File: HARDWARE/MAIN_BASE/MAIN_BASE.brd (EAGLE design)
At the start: 174 x 92.7 mm, 2 parts

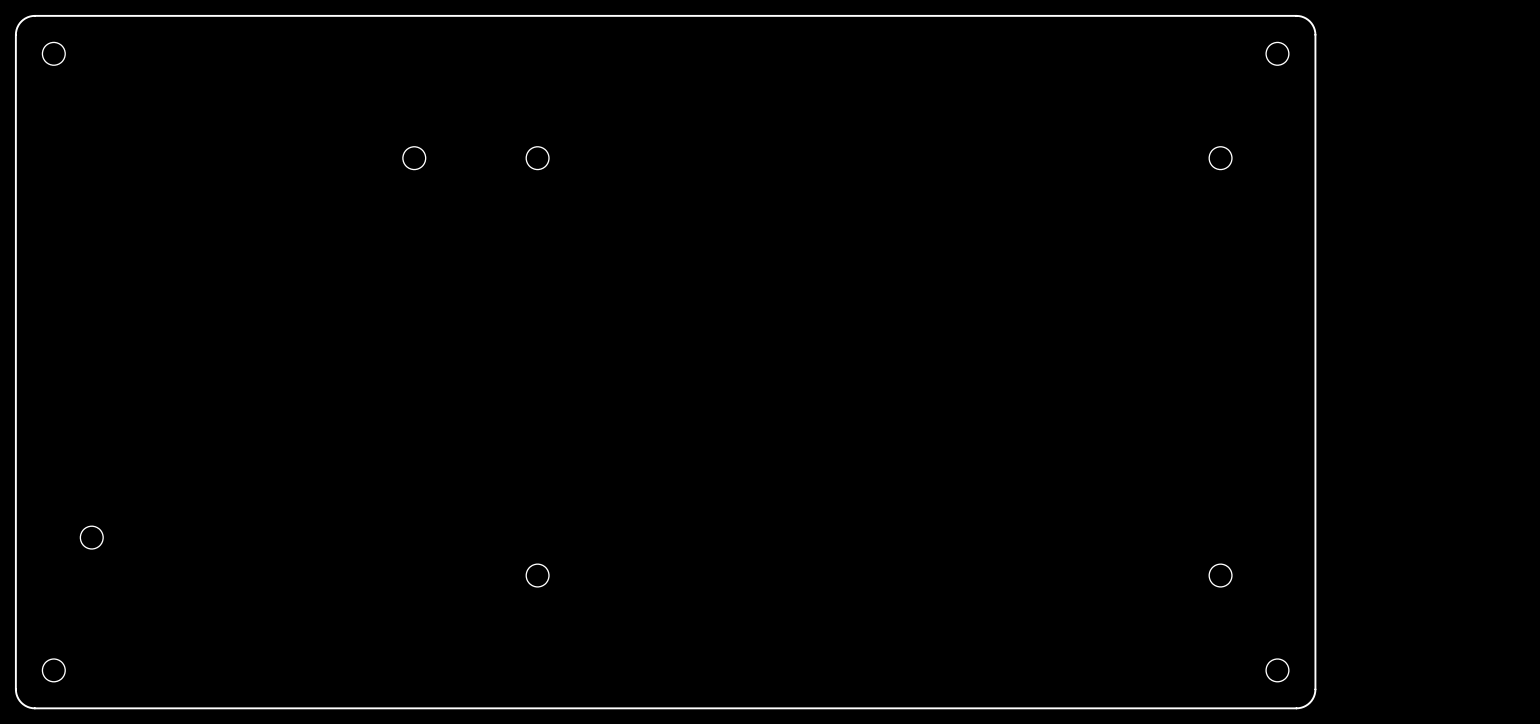
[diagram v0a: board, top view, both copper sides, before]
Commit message: added noisey cricket to base
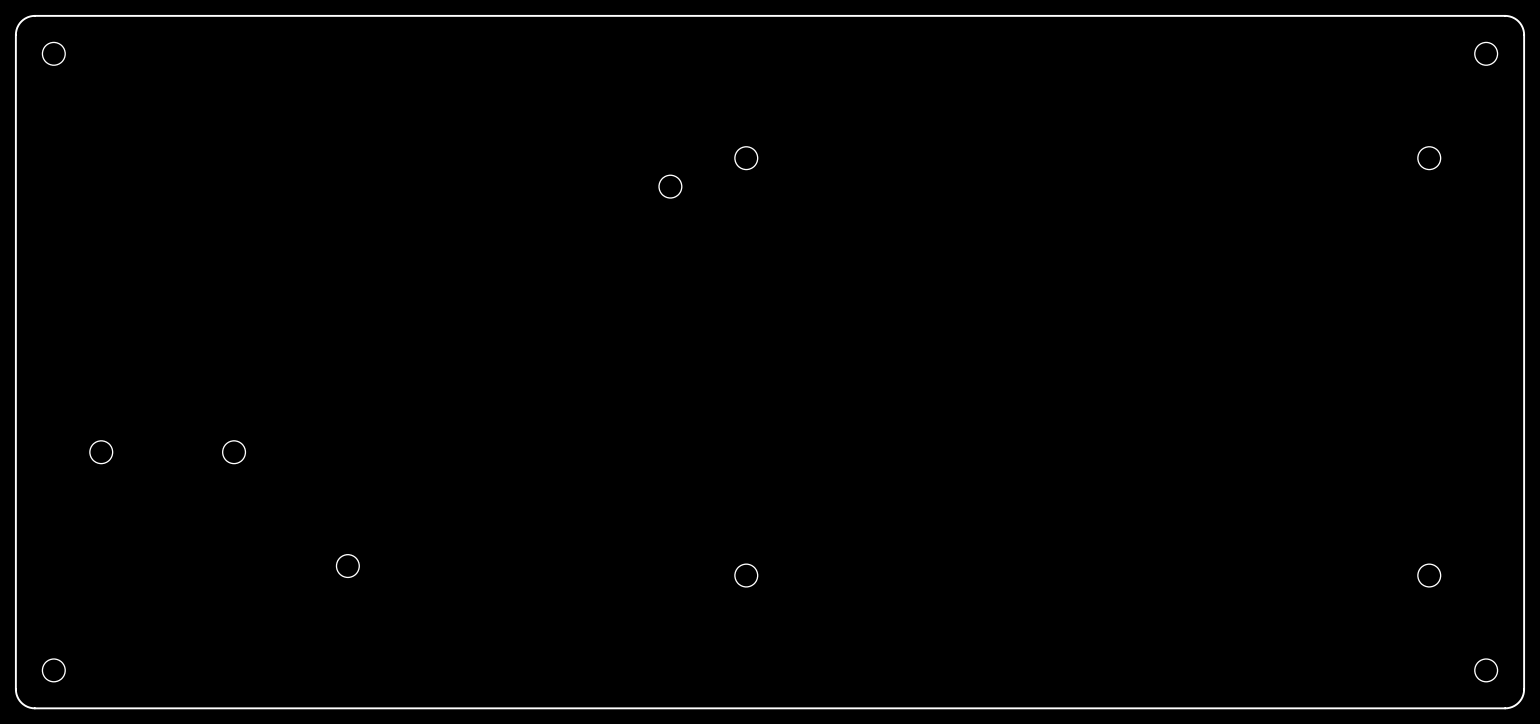
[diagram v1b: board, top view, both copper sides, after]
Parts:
- added E$3: (no value), simon_jumps:NOISY_CRICKET
- moved E$1 32.0 mm to (64.8, 48.3), turned to 180 degrees
- moved E$2 27.9 mm to (142.2, 45.7)
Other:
- board size 174 x 92.7 mm -> 201.9 x 92.7 mm
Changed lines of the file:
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@@
 <board>
 <plain>
-<wire x1="173.99" y1="90.17" x2="173.99" y2="2.54" width="0.254" layer="20"/>
-<wire x1="173.99" y1="2.54" x2="171.45" y2="0" width="0.254" layer="20" curve="-90"/>
-<wire x1="171.45" y1="0" x2="2.54" y2="0" width="0.254" layer="20"/>
+<wire x1="201.93" y1="90.17" x2="201.93" y2="2.54" width="0.254" layer="20"/>
+<wire x1="201.93" y1="2.54" x2="199.39" y2="0" width="0.254" layer="20" curve="-90"/>
+<wire x1="199.39" y1="0" x2="2.54" y2="0" width="0.254" layer="20"/>
 <wire x1="2.54" y1="0" x2="0" y2="2.54" width="0.254" layer="20" curve="-90"/>
 <wire x1="0" y1="2.54" x2="0" y2="90.17" width="0.254" layer="20"/>
 <wire x1="0" y1="90.17" x2="2.54" y2="92.71" width="0.254" layer="20" curve="-90"/>
-<wire x1="2.54" y1="92.71" x2="171.45" y2="92.71" width="0.254" layer="20"/>
-<wire x1="171.45" y1="92.71" x2="173.99" y2="90.17" width="0.254" layer="20" curve="-90"/>
+<wire x1="2.54" y1="92.71" x2="199.39" y2="92.71" width="0.254" layer="20"/>
+<wire x1="199.39" y1="92.71" x2="201.93" y2="90.17" width="0.254" layer="20" curve="-90"/>
 <hole x="5.08" y="87.63" drill="3.048"/>
-<hole x="168.91" y="87.63" drill="3.048"/>
-<hole x="168.91" y="5.08" drill="3.048"/>
+<hole x="196.85" y="87.63" drill="3.048"/>
+<hole x="196.85" y="5.08" drill="3.048"/>
 <hole x="5.08" y="5.08" drill="3.048"/>
 </plain>
@@
 </autorouter>
 <elements>
-<element name="E$1" library="simon_jumps" package="MUSIC_INSTRUMENT_SHIELD" value="" x="33.02" y="44.45"/>
-<element name="E$2" library="simon_jumps" package="SIMON_JUMPS_MAIN_BOARD" value="" x="114.3" y="45.72" rot="R270"/>
+<element name="E$1" library="simon_jumps" package="MUSIC_INSTRUMENT_SHIELD" value="" x="64.77" y="48.26" rot="R180"/>
+<element name="E$2" library="simon_jumps" package="SIMON_JUMPS_MAIN_BOARD" value="" x="142.24" y="45.72" rot="R270"/>
+<element name="E$3" library="simon_jumps" package="NOISY_CRICKET" value="" x="20.32" y="46.99" rot="R270"/>
 </elements>
 <signals>
